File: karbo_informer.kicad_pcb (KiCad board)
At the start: 2 copper layers, 12 parts, among them IC1 MAX7219, IC2 MAX7219, P1 USB_OTG

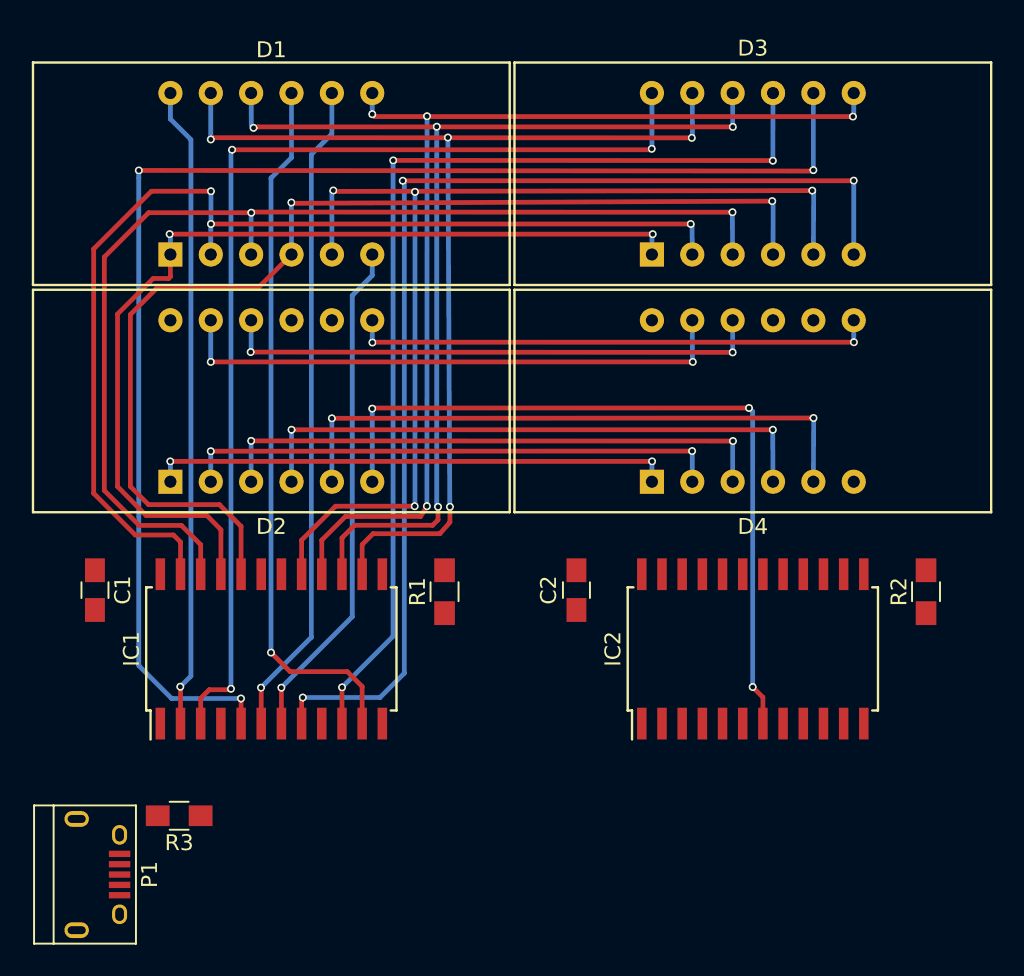
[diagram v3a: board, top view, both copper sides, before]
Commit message: Wire for DIG_2 to MAX7219 in the sell line
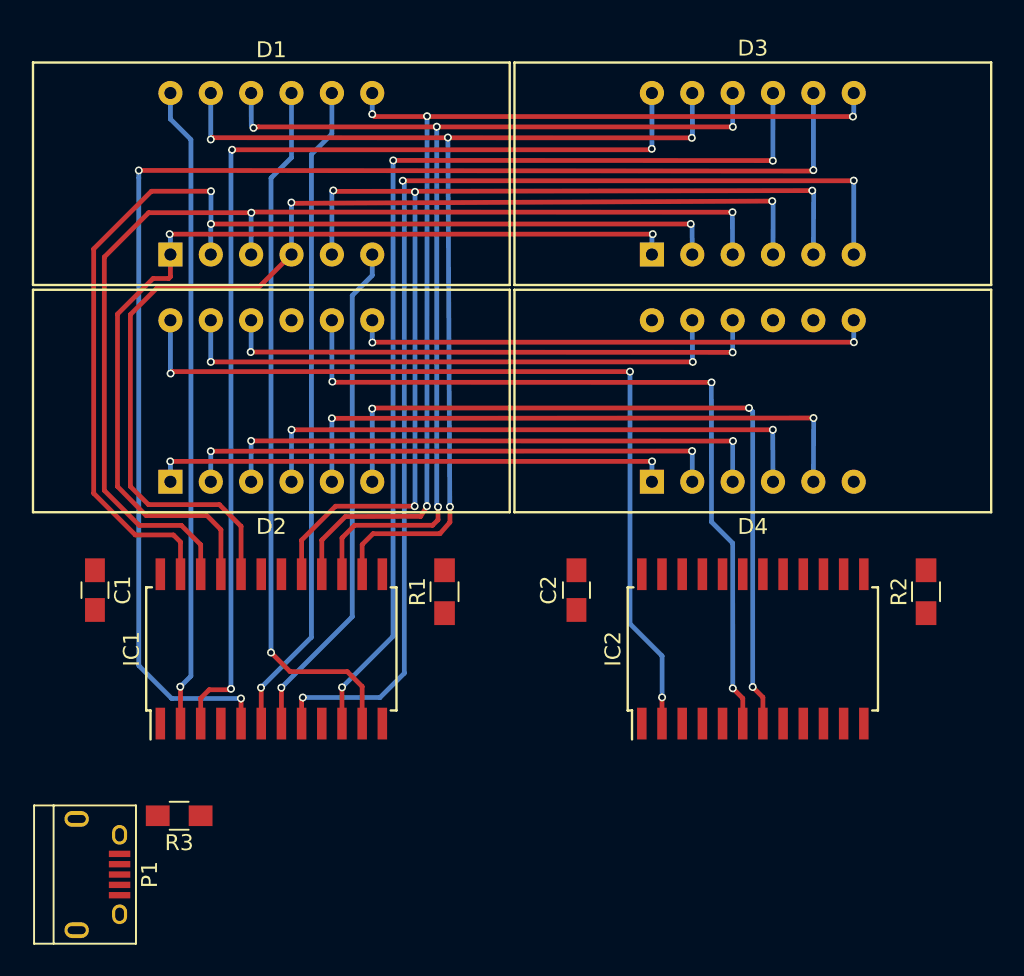
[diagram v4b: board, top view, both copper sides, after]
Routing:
- net /S_DIG_0: track 0.00 -> 55.3 mm, vias 0 -> 3
- net /S_DIG_2: track 0.00 -> 50.0 mm, vias 0 -> 3
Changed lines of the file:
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@@
   (general
     (links 69)
-    (no_connects 36)
+    (no_connects 34)
     (area 23.915 20.025 86.425001 77.825001)
     (thickness 1.6)
     (drawings 0)
-    (tracks 271)
+    (tracks 295)
     (zones 0)
     (modules 12)
@@
   (via (at 67.32 40.74) (size 0.5) (drill 0.3) (layers F.Cu B.Cu) (net 20))
   (segment (start 36.99 40.74) (end 67.32 40.74) (width 0.3) (layer F.Cu) (net 20))
+  (segment (start 34.45 38.12) (end 34.45 41.46) (width 0.3) (layer B.Cu) (net 21) (status 400000))
+  (segment (start 65.385 61.855) (end 65.385 63.5) (width 0.3) (layer F.Cu) (net 21) (status 800000))
+  (segment (start 65.39 61.85) (end 65.385 61.855) (width 0.3) (layer F.Cu) (net 21))
+  (via (at 65.39 61.85) (size 0.5) (drill 0.3) (layers F.Cu B.Cu) (net 21))
+  (segment (start 65.39 59.24) (end 65.39 61.85) (width 0.3) (layer B.Cu) (net 21))
+  (segment (start 63.37 57.22) (end 65.39 59.24) (width 0.3) (layer B.Cu) (net 21))
+  (segment (start 63.37 41.35) (end 63.37 57.22) (width 0.3) (layer B.Cu) (net 21))
+  (via (at 63.37 41.35) (size 0.5) (drill 0.3) (layers F.Cu B.Cu) (net 21))
+  (segment (start 34.58 41.35) (end 63.37 41.35) (width 0.3) (layer F.Cu) (net 21))
+  (segment (start 34.46 41.47) (end 34.58 41.35) (width 0.3) (layer F.Cu) (net 21))
+  (via (at 34.46 41.47) (size 0.5) (drill 0.3) (layers F.Cu B.Cu) (net 21))
+  (segment (start 34.45 41.46) (end 34.46 41.47) (width 0.3) (layer B.Cu) (net 21))
+  (segment (start 44.61 38.12) (end 44.61 41.95) (width 0.3) (layer B.Cu) (net 23) (status 400000))
+  (segment (start 70.47 61.91) (end 70.465 63.5) (width 0.3) (layer F.Cu) (net 23) (status 800000))
+  (segment (start 69.84 61.28) (end 70.47 61.91) (width 0.3) (layer F.Cu) (net 23))
+  (via (at 69.84 61.28) (size 0.5) (drill 0.3) (layers F.Cu B.Cu) (net 23))
+  (segment (start 69.83 52.14) (end 69.84 61.28) (width 0.3) (layer B.Cu) (net 23))
+  (segment (start 68.5 50.81) (end 69.83 52.14) (width 0.3) (layer B.Cu) (net 23))
+  (segment (start 68.49 42.03) (end 68.5 50.81) (width 0.3) (layer B.Cu) (net 23))
+  (via (at 68.5 42.03) (size 0.5) (drill 0.3) (layers F.Cu B.Cu) (net 23))
+  (segment (start 44.68 42.02) (end 68.5 42.03) (width 0.3) (layer F.Cu) (net 23))
+  (segment (start 44.64 41.98) (end 44.68 42.02) (width 0.3) (layer F.Cu) (net 23))
+  (via (at 44.64 41.98) (size 0.5) (drill 0.3) (layers F.Cu B.Cu) (net 23))
+  (segment (start 44.61 41.95) (end 44.64 41.98) (width 0.3) (layer B.Cu) (net 23))
   (segment (start 47.15 38.12) (end 47.15 39.51) (width 0.3) (layer B.Cu) (net 24))
   (segment (start 77.45 39.49) (end 77.45 38.12) (width 0.3) (layer B.Cu) (net 24))

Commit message: Wire for DIG_1 to MAX7219 in the sell line
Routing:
- net /S_DIG_1: track 0.00 -> 60.0 mm, vias 0 -> 3
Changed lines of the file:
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@@
   (general
     (links 69)
-    (no_connects 34)
+    (no_connects 33)
     (area 23.915 20.025 86.425001 77.825001)
     (thickness 1.6)
     (drawings 0)
-    (tracks 295)
+    (tracks 306)
     (zones 0)
     (modules 12)
@@
   (via (at 34.46 41.47) (size 0.5) (drill 0.3) (layers F.Cu B.Cu) (net 21))
   (segment (start 34.45 41.46) (end 34.46 41.47) (width 0.3) (layer B.Cu) (net 21))
+  (segment (start 42.07 38.12) (end 42.07 42.81) (width 0.3) (layer B.Cu) (net 22) (status 400000))
+  (segment (start 76.815 61.895) (end 76.815 63.5) (width 0.3) (layer F.Cu) (net 22) (status 800000))
+  (segment (start 76.14 61.22) (end 76.815 61.895) (width 0.3) (layer F.Cu) (net 22))
+  (via (at 76.14 61.22) (size 0.5) (drill 0.3) (layers F.Cu B.Cu) (net 22))
+  (segment (start 76.14 42.71) (end 76.14 61.22) (width 0.3) (layer B.Cu) (net 22))
+  (segment (start 76.18 42.67) (end 76.14 42.71) (width 0.3) (layer B.Cu) (net 22))
+  (via (at 76.18 42.67) (size 0.5) (drill 0.3) (layers F.Cu B.Cu) (net 22))
+  (segment (start 42.21 42.67) (end 76.18 42.67) (width 0.3) (layer F.Cu) (net 22))
+  (segment (start 42.05 42.83) (end 42.21 42.67) (width 0.3) (layer F.Cu) (net 22))
+  (via (at 42.05 42.83) (size 0.5) (drill 0.3) (layers F.Cu B.Cu) (net 22))
+  (segment (start 42.07 42.81) (end 42.05 42.83) (width 0.3) (layer B.Cu) (net 22))
   (segment (start 44.61 38.12) (end 44.61 41.95) (width 0.3) (layer B.Cu) (net 23) (status 400000))
   (segment (start 70.47 61.91) (end 70.465 63.5) (width 0.3) (layer F.Cu) (net 23) (status 800000))

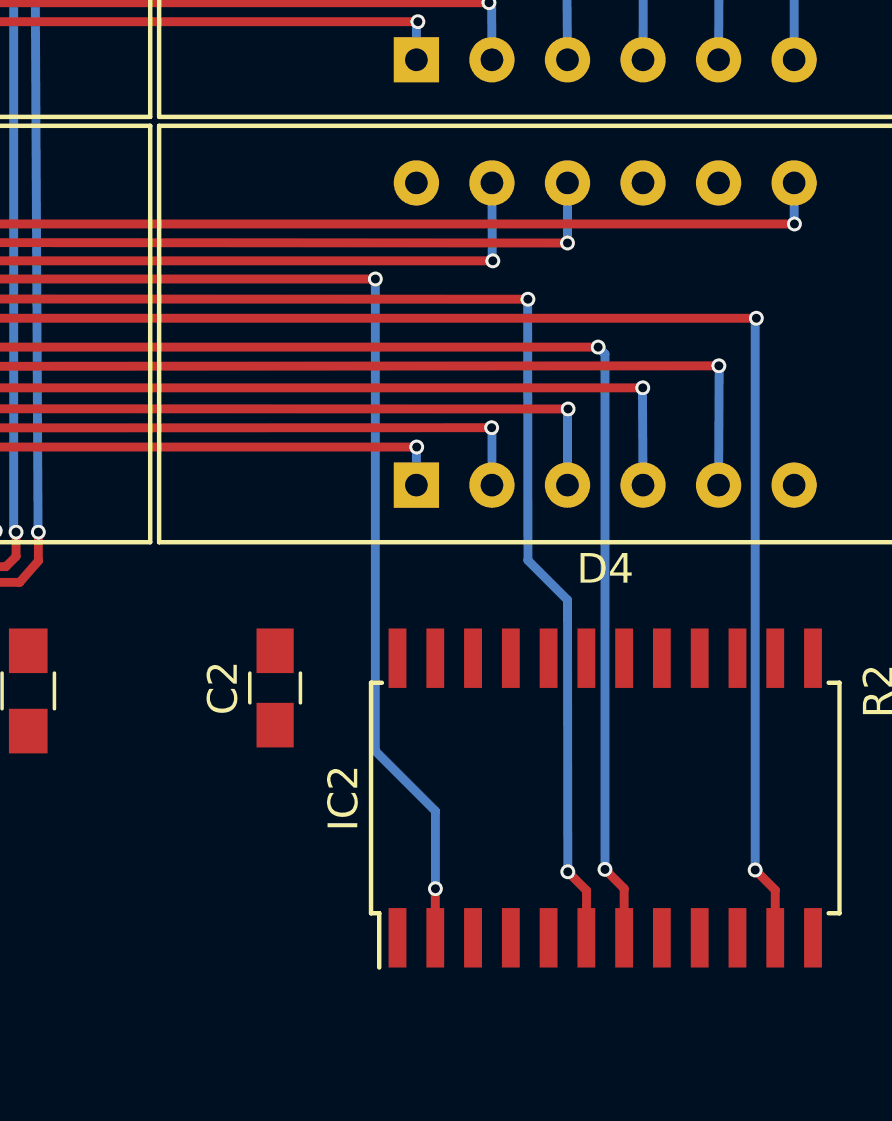
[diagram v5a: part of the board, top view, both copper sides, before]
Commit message: Wire for DIG_4 to MAX7219 in the sell line
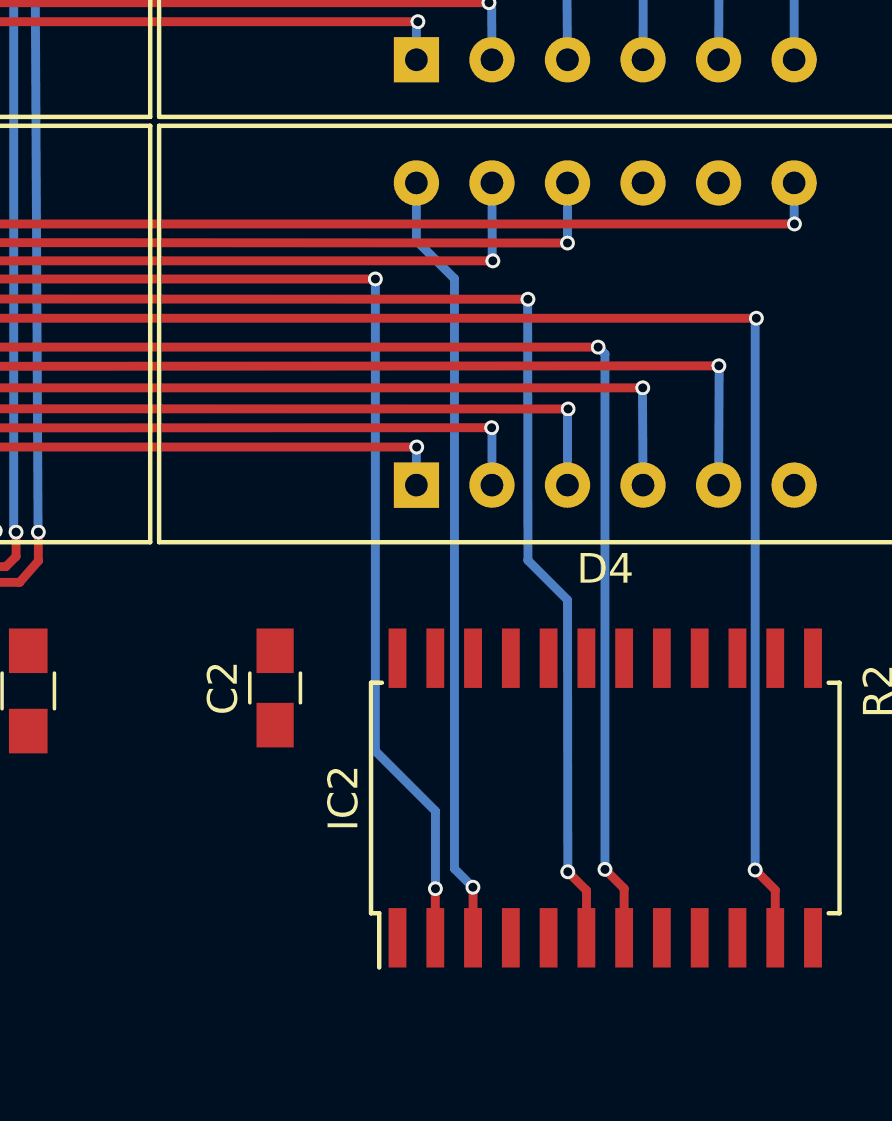
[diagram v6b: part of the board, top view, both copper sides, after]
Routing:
- net /S_DIG_4: track 0.00 -> 26.2 mm, vias 0 -> 1
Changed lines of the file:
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@@
   (general
     (links 69)
-    (no_connects 33)
+    (no_connects 32)
     (area 23.915 20.025 86.425001 77.825001)
     (thickness 1.6)
     (drawings 0)
-    (tracks 306)
+    (tracks 313)
     (zones 0)
     (modules 12)
@@
   (segment (start 48.47 28.06) (end 48.46 28.07) (width 0.3) (layer B.Cu) (net 27))
   (segment (start 72.37 23.82) (end 72.36 28.08) (width 0.3) (layer B.Cu) (net 27))
+  (segment (start 64.75 38.12) (end 64.75 40.06) (width 0.3) (layer B.Cu) (net 29) (status 400000))
+  (segment (start 66.655 61.805) (end 66.655 63.5) (width 0.3) (layer F.Cu) (net 29) (status 800000))
+  (segment (start 66.65 61.8) (end 66.655 61.805) (width 0.3) (layer F.Cu) (net 29))
+  (via (at 66.65 61.8) (size 0.5) (drill 0.3) (layers F.Cu B.Cu) (net 29))
+  (segment (start 66.03 61.18) (end 66.65 61.8) (width 0.3) (layer B.Cu) (net 29))
+  (segment (start 66.03 41.34) (end 66.03 61.18) (width 0.3) (layer B.Cu) (net 29))
+  (segment (start 64.75 40.06) (end 66.03 41.34) (width 0.3) (layer B.Cu) (net 29))
   (segment (start 77.45 33.98) (end 77.45 29.33) (width 0.3) (layer B.Cu) (net 33))
   (segment (start 42.705 61.935) (end 42.705 63.5) (width 0.3) (layer F.Cu) (net 33))

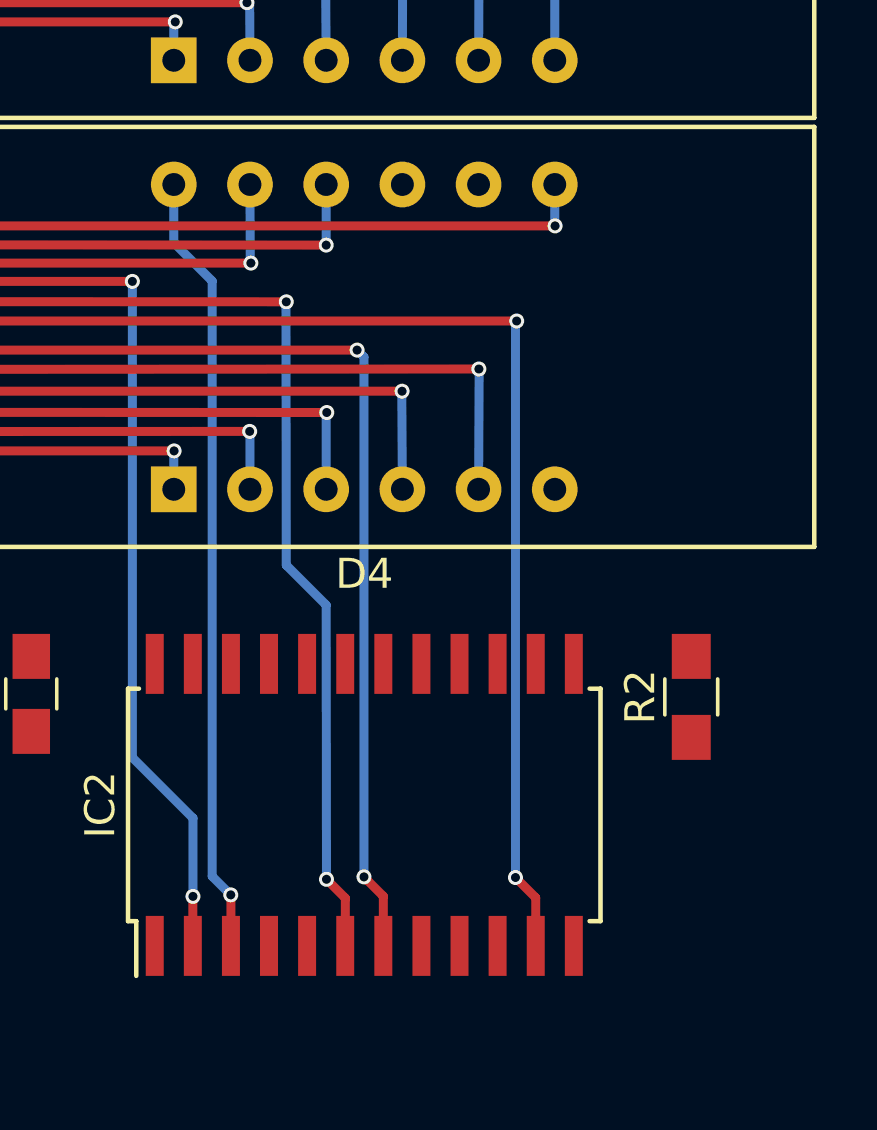
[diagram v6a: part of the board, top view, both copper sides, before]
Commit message: Wire for DIG_5 to MAX7219 in the sell line
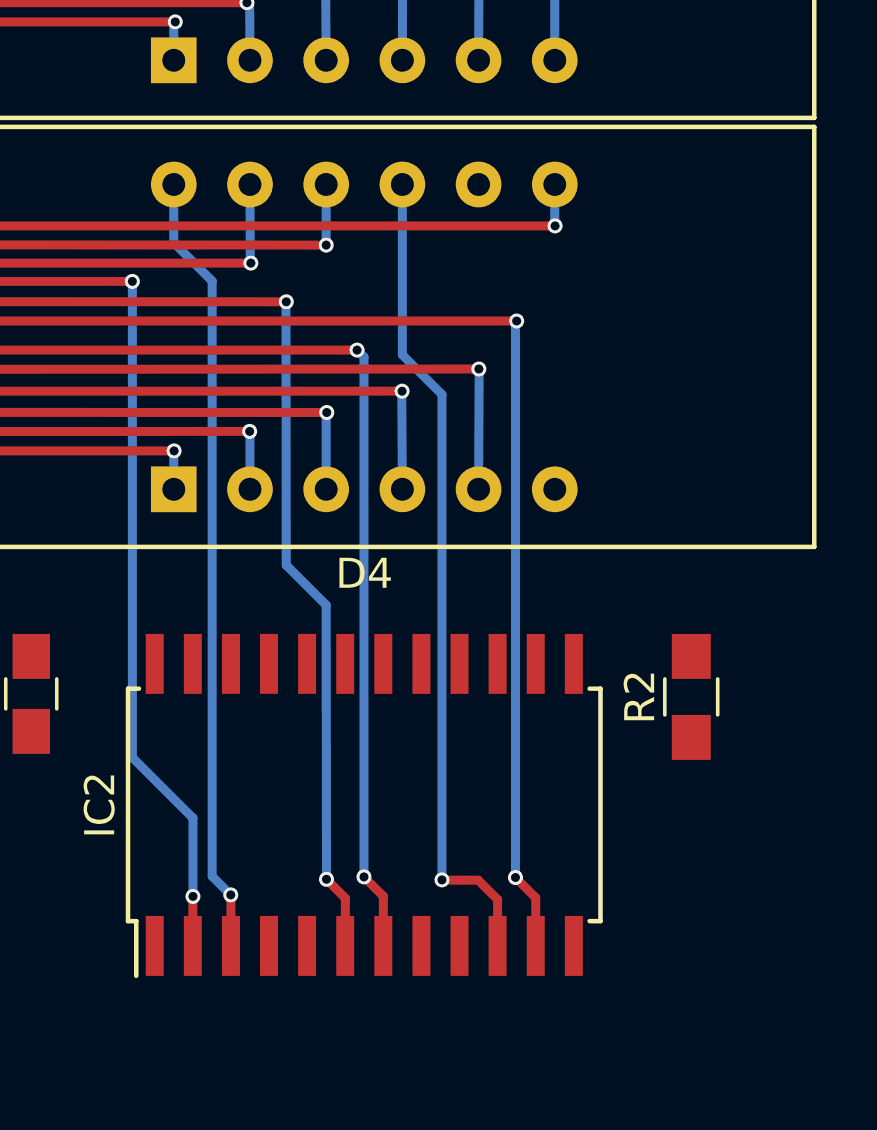
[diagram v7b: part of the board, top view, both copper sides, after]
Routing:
- net /S_DIG_5: track 0.00 -> 27.4 mm, vias 0 -> 1
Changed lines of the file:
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@@
   (general
     (links 69)
-    (no_connects 32)
+    (no_connects 31)
     (area 23.915 20.025 86.425001 77.825001)
     (thickness 1.6)
     (drawings 0)
-    (tracks 313)
+    (tracks 321)
     (zones 0)
     (modules 12)
@@
   (segment (start 66.03 41.34) (end 66.03 61.18) (width 0.3) (layer B.Cu) (net 29))
   (segment (start 64.75 40.06) (end 66.03 41.34) (width 0.3) (layer B.Cu) (net 29))
+  (segment (start 72.37 38.12) (end 72.37 43.8) (width 0.3) (layer B.Cu) (net 30) (status 400000))
+  (segment (start 75.545 61.955) (end 75.545 63.5) (width 0.3) (layer F.Cu) (net 30) (status 800000))
+  (segment (start 74.9 61.31) (end 75.545 61.955) (width 0.3) (layer F.Cu) (net 30))
+  (segment (start 73.7 61.31) (end 74.9 61.31) (width 0.3) (layer F.Cu) (net 30))
+  (segment (start 73.69 61.3) (end 73.7 61.31) (width 0.3) (layer F.Cu) (net 30))
+  (via (at 73.69 61.3) (size 0.5) (drill 0.3) (layers F.Cu B.Cu) (net 30))
+  (segment (start 73.69 45.12) (end 73.69 61.3) (width 0.3) (layer B.Cu) (net 30))
+  (segment (start 72.37 43.8) (end 73.69 45.12) (width 0.3) (layer B.Cu) (net 30))
   (segment (start 77.45 33.98) (end 77.45 29.33) (width 0.3) (layer B.Cu) (net 33))
   (segment (start 42.705 61.935) (end 42.705 63.5) (width 0.3) (layer F.Cu) (net 33))
